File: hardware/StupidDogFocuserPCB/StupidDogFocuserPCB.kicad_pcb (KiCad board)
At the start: 2 copper layers, 68.6 x 53.3 mm, 18 parts, among them M1 Stepper_Motor_bipolar, SW1 Rotary_Encoder_Switch, U1 DHT11, U2 SN74HC14N

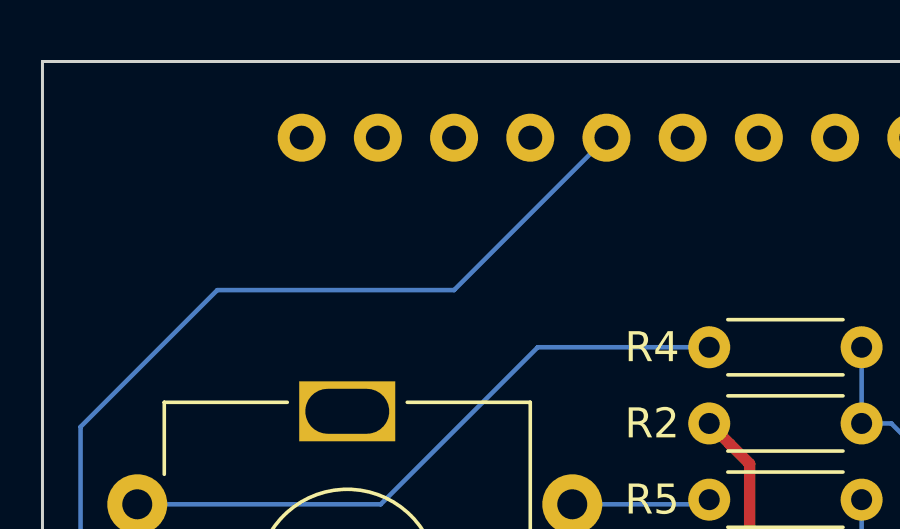
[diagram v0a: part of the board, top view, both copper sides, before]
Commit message: moved dht pin.
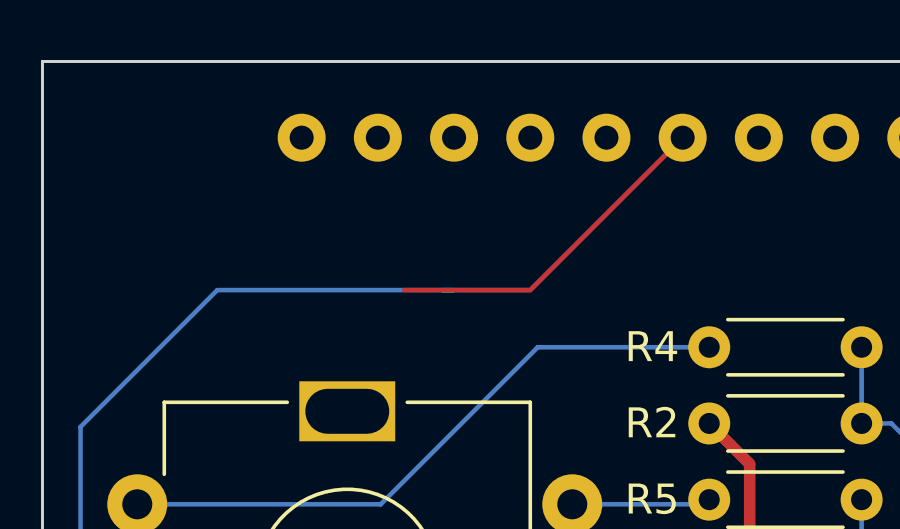
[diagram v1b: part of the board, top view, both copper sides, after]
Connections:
- A2 pad 27: (no net) -> DHT
- A2 pad 28: DHT -> (no net)
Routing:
- net DHT: track 44.8 -> 59.1 mm
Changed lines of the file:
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@@
     (thickness 1.6)
     (drawings 27)
-    (tracks 116)
+    (tracks 120)
     (zones 0)
     (modules 18)
@@
   )
   (setup
-    (last_trace_width 0.381)
+    (last_trace_width 0.1524)
     (user_trace_width 0.1524)
     (user_trace_width 0.381)
@@
     (add_net GND)
     (add_net HalfStep)
-    (add_net "Net-(A1-Pad11)")
-    (add_net "Net-(A1-Pad12)")
-    (add_net "Net-(A1-Pad2)")
-    (add_net "Net-(A2-Pad1)")
-    (add_net "Net-(A2-Pad10)")
-    (add_net "Net-(A2-Pad11)")
-    (add_net "Net-(A2-Pad12)")
-    (add_net "Net-(A2-Pad15)")
-    (add_net "Net-(A2-Pad16)")
-    (add_net "Net-(A2-Pad19)")
-    (add_net "Net-(A2-Pad2)")
-    (add_net "Net-(A2-Pad23)")
-    (add_net "Net-(A2-Pad24)")
-    (add_net "Net-(A2-Pad25)")
-    (add_net "Net-(A2-Pad26)")
-    (add_net "Net-(A2-Pad27)")
-    (add_net "Net-(A2-Pad3)")
-    (add_net "Net-(A2-Pad30)")
-    (add_net "Net-(A2-Pad31)")
-    (add_net "Net-(A2-Pad32)")
-    (add_net "Net-(A2-Pad4)")
-    (add_net "Net-(A2-Pad9)")
     (add_net "Net-(R3-Pad2)")
     (add_net "Net-(R4-Pad2)")
     (add_net "Net-(R5-Pad1)")
-    (add_net "Net-(U1-Pad3)")
-    (add_net "Net-(U2-Pad10)")
-    (add_net "Net-(U2-Pad11)")
-    (add_net "Net-(U2-Pad12)")
-    (add_net "Net-(U2-Pad13)")
-    (add_net "Net-(U2-Pad8)")
-    (add_net "Net-(U2-Pad9)")
     (add_net SW)
     (add_net SW_A)
@@
     (pad 13 thru_hole oval (at 33.02 0 270) (size 1.6 1.6) (drill 0.8) (layers *.Cu *.Mask)
       (net 4 HalfStep))
-    (pad 28 thru_hole oval (at 1.02 -48.26 270) (size 1.6 1.6) (drill 0.8) (layers *.Cu *.Mask)
+    (pad 28 thru_hole oval (at 1.02 -48.26 270) (size 1.6 1.6) (drill 0.8) (layers *.Cu *.Mask))
+    (pad 12 thru_hole oval (at 30.48 0 270) (size 1.6 1.6) (drill 0.8) (layers *.Cu *.Mask))
+    (pad 27 thru_hole oval (at 3.56 -48.26 270) (size 1.6 1.6) (drill 0.8) (layers *.Cu *.Mask)
       (net 2 DHT))
-    (pad 12 thru_hole oval (at 30.48 0 270) (size 1.6 1.6) (drill 0.8) (layers *.Cu *.Mask))
-    (pad 27 thru_hole oval (at 3.56 -48.26 270) (size 1.6 1.6) (drill 0.8) (layers *.Cu *.Mask))
     (pad 11 thru_hole oval (at 27.94 0 270) (size 1.6 1.6) (drill 0.8) (layers *.Cu *.Mask))
     (pad 26 thru_hole oval (at 6.1 -48.26 270) (size 1.6 1.6) (drill 0.8) (layers *.Cu *.Mask))
@@
   (segment (start 99.580001 85.610001) (end 100.33 86.36) (width 0.1524) (layer B.Cu) (net 2))
   (segment (start 99.153279 82.536599) (end 99.046599 82.643279) (width 0.1524) (layer B.Cu) (net 2))
-  (segment (start 119.13 64.77) (end 111.238335 64.77) (width 0.1524) (layer B.Cu) (net 2))
   (segment (start 99.046599 85.076599) (end 99.580001 85.610001) (width 0.1524) (layer B.Cu) (net 2))
   (segment (start 103.518401 82.536599) (end 99.153279 82.536599) (width 0.1524) (layer B.Cu) (net 2))
-  (segment (start 124.21 59.69) (end 119.13 64.77) (width 0.1524) (layer B.Cu) (net 2))
   (segment (start 99.046599 82.643279) (end 99.046599 85.076599) (width 0.1524) (layer B.Cu) (net 2))
   (segment (start 106.68 79.375) (end 103.518401 82.536599) (width 0.1524) (layer B.Cu) (net 2))
   (segment (start 111.238335 64.77) (end 106.68 69.328335) (width 0.1524) (layer B.Cu) (net 2))
   (segment (start 106.68 69.328335) (end 106.68 79.375) (width 0.1524) (layer B.Cu) (net 2))
+  (segment (start 126.75 59.69) (end 121.67 64.77) (width 0.1524) (layer F.Cu) (net 2))
+  (segment (start 121.67 64.77) (end 117.475 64.77) (width 0.1524) (layer F.Cu) (net 2))
+  (segment (start 121.67 64.77) (end 126.75 59.69) (width 0.1524) (layer B.Cu) (net 2))
+  (segment (start 119.13 64.77) (end 118.745 64.77) (width 0.1524) (layer B.Cu) (net 2))
+  (segment (start 118.745 64.77) (end 121.67 64.77) (width 0.1524) (layer B.Cu) (net 2))
+  (segment (start 118.745 64.77) (end 111.238335 64.77) (width 0.1524) (layer B.Cu) (net 2))
   (segment (start 140.97 106.68) (end 137.16 102.87) (width 0.635) (layer B.Cu) (net 3))
   (segment (start 140.97 107.95) (end 140.97 106.68) (width 0.635) (layer B.Cu) (net 3))

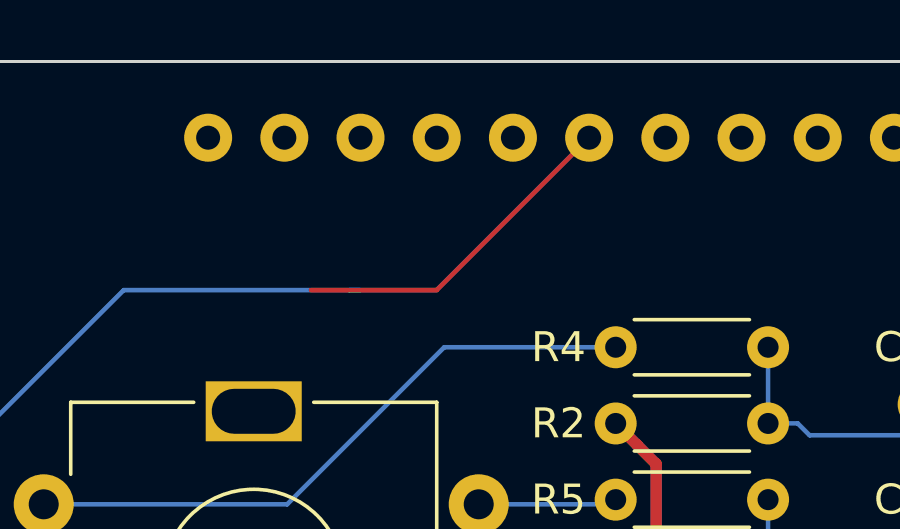
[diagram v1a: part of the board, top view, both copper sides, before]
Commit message: erant trace removed
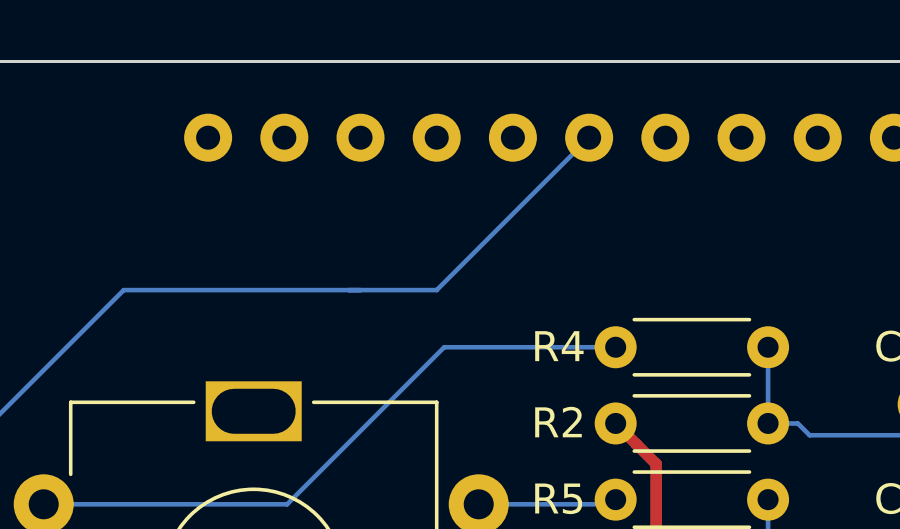
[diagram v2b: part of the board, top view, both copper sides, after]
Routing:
- net DHT: track 59.1 -> 47.7 mm
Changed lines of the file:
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@@
     (thickness 1.6)
     (drawings 27)
-    (tracks 120)
+    (tracks 118)
     (zones 0)
     (modules 18)
@@
   (segment (start 111.238335 64.77) (end 106.68 69.328335) (width 0.1524) (layer B.Cu) (net 2))
   (segment (start 106.68 69.328335) (end 106.68 79.375) (width 0.1524) (layer B.Cu) (net 2))
-  (segment (start 126.75 59.69) (end 121.67 64.77) (width 0.1524) (layer F.Cu) (net 2))
-  (segment (start 121.67 64.77) (end 117.475 64.77) (width 0.1524) (layer F.Cu) (net 2))
   (segment (start 121.67 64.77) (end 126.75 59.69) (width 0.1524) (layer B.Cu) (net 2))
   (segment (start 119.13 64.77) (end 118.745 64.77) (width 0.1524) (layer B.Cu) (net 2))

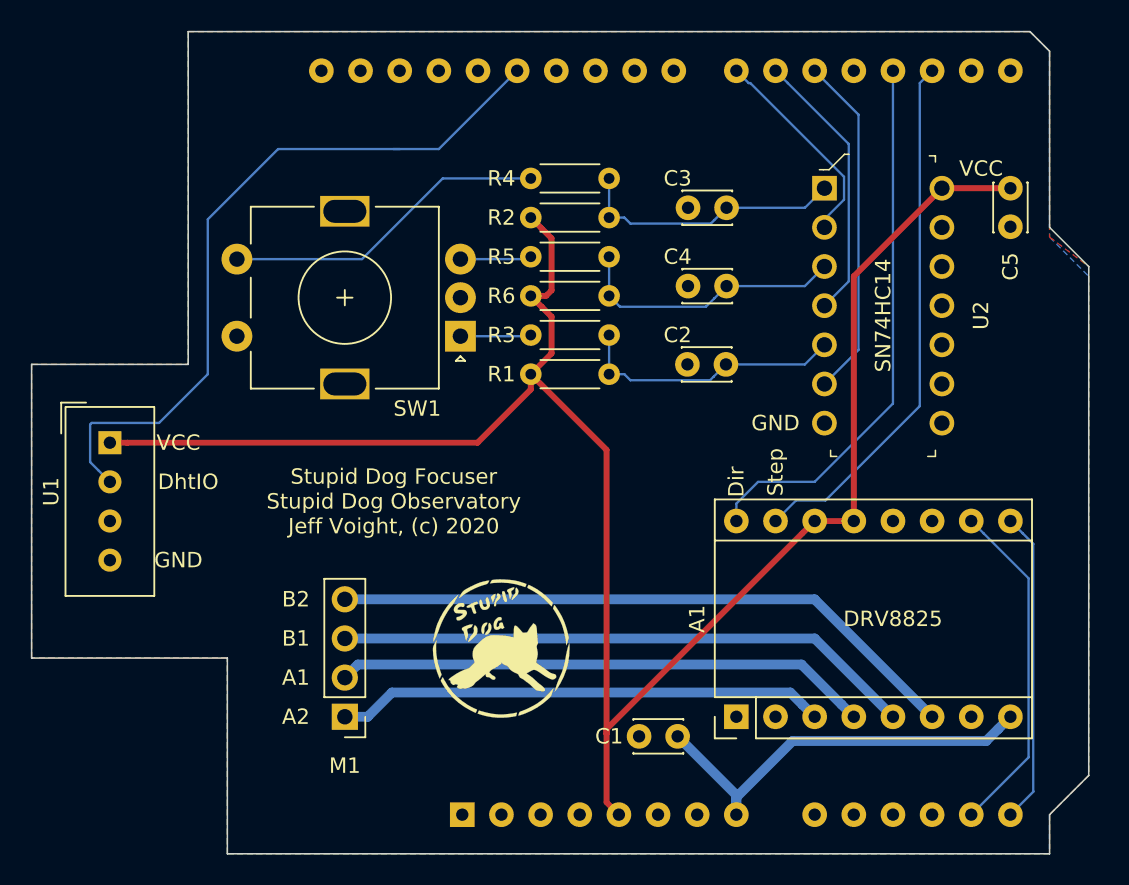
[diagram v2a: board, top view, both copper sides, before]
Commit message: thicker traces
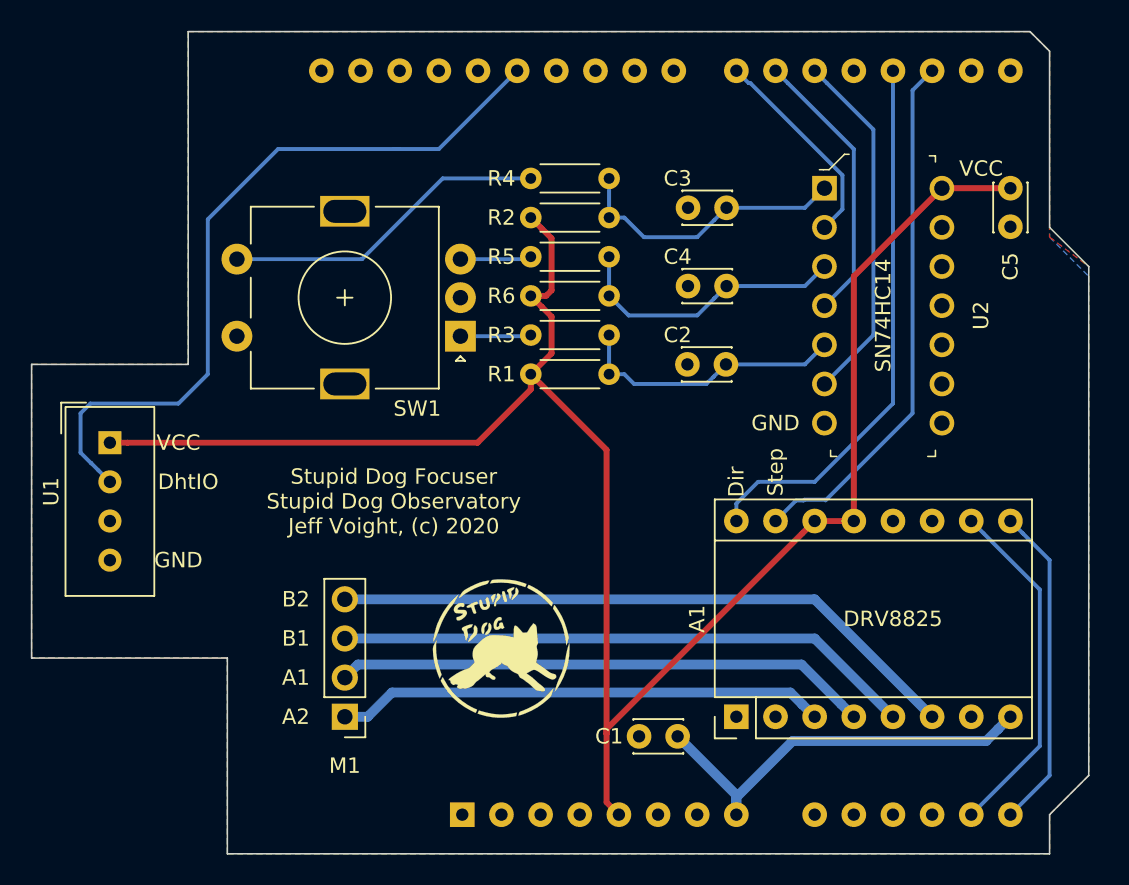
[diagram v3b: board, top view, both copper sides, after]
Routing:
- net DHT: track 47.7 -> 49.0 mm
- net ~Enable: track 20.3 -> 21.2 mm
- net ENCA_A: track 22.4 -> 23.2 mm
- net SW: track 17.6 -> 18.4 mm
- net HalfStep: track 22.1 -> 22.7 mm

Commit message: added m1 and m2
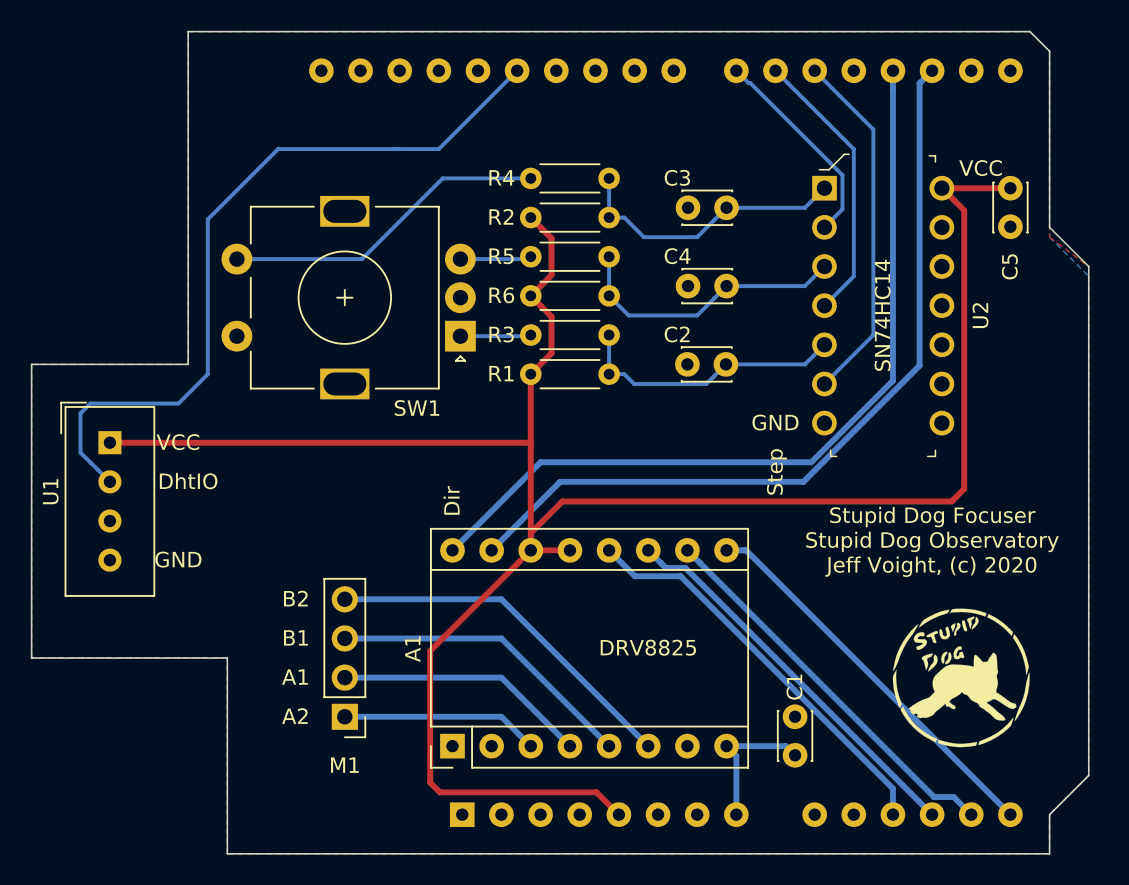
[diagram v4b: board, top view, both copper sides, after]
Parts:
- moved G*** 29.9 mm to (155.6, 99.1)
- moved A1 18.5 mm to (122.6, 103.5)
- moved C1 10.2 mm to (144.8, 101.6), turned to 270 degrees
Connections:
- net HalfStep renamed M0
- A1 pad 11: (no net) -> M1
- A1 pad 12: (no net) -> M2
- A2 pad 11: (no net) -> M2
- A2 pad 12: (no net) -> M1
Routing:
- net M2: track 0.00 -> 26.5 mm
- net M1: track 0.00 -> 25.5 mm
- net A2: track 31.8 -> 12.9 mm
- net VDD: track 27.7 -> 9.40 mm
- net A1: track 34.8 -> 16.4 mm
- net Dir: track 35.6 -> 53.2 mm
- net B1: track 37.7 -> 20.0 mm
- net B2: track 41.3 -> 23.6 mm
- net Step: track 34.6 -> 52.2 mm
- net VCC: track 124.0 -> 139.5 mm
- net ~Enable: track 21.2 -> 25.5 mm
- net M0: track 22.7 -> 25.5 mm

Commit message: gerbers
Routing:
- net SW_A: track 13.6 -> 14.3 mm
